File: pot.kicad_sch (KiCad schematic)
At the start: 1 part

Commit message: started to work on power part
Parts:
- gave numbers to parts that had none: 1
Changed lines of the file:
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@@
   (symbol (lib_id "power:GND") (at 112.395 92.075 0) (unit 1)
     (in_bom yes) (on_board yes) (fields_autoplaced)
-    (property "Reference" "#PWR?" (id 0) (at 112.395 98.425 0)
+    (property "Reference" "#PWR034" (id 0) (at 112.395 98.425 0)
       (effects (font (size 1.27 1.27)) hide)
     )
@@
   (symbol (lib_id "eurorack:Pot_500") (at 112.395 86.995 0) (unit 1)
     (in_bom yes) (on_board yes) (fields_autoplaced)
-    (property "Reference" "RV?" (id 0) (at 110.49 85.7249 0)
+    (property "Reference" "RV3" (id 0) (at 110.49 85.7249 0)
       (effects (font (size 1.27 1.27)) (justify right))
     )
@@
   (symbol (lib_id "eurorack:+2V048") (at 112.395 81.915 0) (unit 1)
     (in_bom yes) (on_board yes) (fields_autoplaced)
-    (property "Reference" "#PWR?" (id 0) (at 112.395 79.375 0)
+    (property "Reference" "#PWR033" (id 0) (at 112.395 79.375 0)
       (effects (font (size 1.27 1.27)) hide)
     )

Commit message: working on powers
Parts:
- renumbered RV3 to RV10
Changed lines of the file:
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@@
     (effects (font (size 1.27 1.27)) (justify left))
   )
-  (symbol (lib_id "power:GND") (at 112.395 92.075 0) (unit 1)
+  (symbol (lib_id "power:GND") (at 112.395 92.075 0)
     (in_bom yes) (on_board yes) (fields_autoplaced)
-    (property "Reference" "#PWR034" (id 0) (at 112.395 98.425 0)
+    (property "Reference" "#PWR048" (id 0) (at 112.395 98.425 0)
       (effects (font (size 1.27 1.27)) hide)
     )
@@
     (pin "1")
   )
-  (symbol (lib_id "eurorack:Pot_500") (at 112.395 86.995 0) (unit 1)
+  (symbol (lib_id "eurorack:Pot_500") (at 112.395 86.995 0)
     (in_bom yes) (on_board yes) (fields_autoplaced)
-    (property "Reference" "RV3" (id 0) (at 110.49 85.7249 0)
+    (property "Reference" "RV10" (id 0) (at 110.49 85.7249 0)
       (effects (font (size 1.27 1.27)) (justify right))
     )
@@
     (pin "3")
   )
-  (symbol (lib_id "eurorack:+2V048") (at 112.395 81.915 0) (unit 1)
+  (symbol (lib_id "eurorack:+2V048") (at 112.395 81.915 0)
     (in_bom yes) (on_board yes) (fields_autoplaced)
-    (property "Reference" "#PWR033" (id 0) (at 112.395 79.375 0)
+    (property "Reference" "#PWR047" (id 0) (at 112.395 79.375 0)
       (effects (font (size 1.27 1.27)) hide)
     )

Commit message: WIP
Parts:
- renumbered RV10 to RV3
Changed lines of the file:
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@@
     (effects (font (size 1.27 1.27)) (justify left))
   )
-  (symbol (lib_id "power:GND") (at 112.395 92.075 0)
+  (symbol (lib_id "power:GND") (at 112.395 92.075 0) (unit 1)
     (in_bom yes) (on_board yes) (fields_autoplaced)
-    (property "Reference" "#PWR048" (id 0) (at 112.395 98.425 0)
+    (property "Reference" "#PWR034" (id 0) (at 112.395 98.425 0)
       (effects (font (size 1.27 1.27)) hide)
     )
@@
     (pin "1")
   )
-  (symbol (lib_id "eurorack:Pot_500") (at 112.395 86.995 0)
+  (symbol (lib_id "eurorack:Pot_500") (at 112.395 86.995 0) (unit 1)
     (in_bom yes) (on_board yes) (fields_autoplaced)
-    (property "Reference" "RV10" (id 0) (at 110.49 85.7249 0)
+    (property "Reference" "RV3" (id 0) (at 110.49 85.7249 0)
       (effects (font (size 1.27 1.27)) (justify right))
     )
@@
     (pin "3")
   )
-  (symbol (lib_id "eurorack:+2V048") (at 112.395 81.915 0)
+  (symbol (lib_id "eurorack:+2V048") (at 112.395 81.915 0) (unit 1)
     (in_bom yes) (on_board yes) (fields_autoplaced)
-    (property "Reference" "#PWR047" (id 0) (at 112.395 79.375 0)
+    (property "Reference" "#PWR033" (id 0) (at 112.395 79.375 0)
       (effects (font (size 1.27 1.27)) hide)
     )

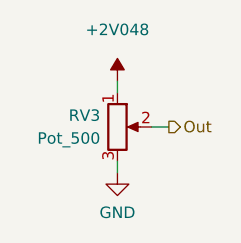
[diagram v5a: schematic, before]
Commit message: cleaning into modules
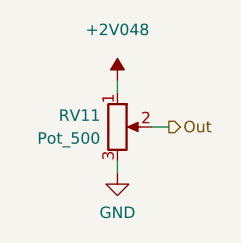
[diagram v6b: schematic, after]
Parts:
- renumbered RV3 to RV11
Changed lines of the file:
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@@
     (effects (font (size 1.27 1.27)) (justify left))
   )
-  (symbol (lib_id "power:GND") (at 112.395 92.075 0) (unit 1)
+  (symbol (lib_id "power:GND") (at 112.395 92.075 0)
     (in_bom yes) (on_board yes) (fields_autoplaced)
-    (property "Reference" "#PWR040" (id 0) (at 112.395 98.425 0)
+    (property "Reference" "#PWR083" (id 0) (at 112.395 98.425 0)
       (effects (font (size 1.27 1.27)) hide)
     )
@@
     (pin "1")
   )
-  (symbol (lib_id "eurorack:Pot_500") (at 112.395 86.995 0) (unit 1)
+  (symbol (lib_id "eurorack:Pot_500") (at 112.395 86.995 0)
     (in_bom yes) (on_board yes) (fields_autoplaced)
-    (property "Reference" "RV3" (id 0) (at 110.49 85.7249 0)
+    (property "Reference" "RV11" (id 0) (at 110.49 85.7249 0)
       (effects (font (size 1.27 1.27)) (justify right))
     )
@@
     (pin "3")
   )
-  (symbol (lib_id "eurorack:+2V048") (at 112.395 81.915 0) (unit 1)
+  (symbol (lib_id "eurorack:+2V048") (at 112.395 81.915 0)
     (in_bom yes) (on_board yes) (fields_autoplaced)
-    (property "Reference" "#PWR039" (id 0) (at 112.395 79.375 0)
+    (property "Reference" "#PWR082" (id 0) (at 112.395 79.375 0)
       (effects (font (size 1.27 1.27)) hide)
     )

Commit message: working on AD inputs
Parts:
- added D26: BAS 85 VIS, Diode_SMD:D_MiniMELF, symbol eurorack:BAS 85 VIS
- added R60: R-10k-1206, Resistor_SMD:R_1206_3216Metric_Pad1.30x1.75mm_HandSolder, symbol eurorack:R-10k-1206
- added R61: R-2k-1206, Resistor_SMD:R_1206_3216Metric_Pad1.30x1.75mm_HandSolder, symbol eurorack:R-2k-1206
- added U25: LUM-1502-03_3.5mm_mono_vertical_jack, eurorack:LUM 1502-03, symbol eurorack:LUM-1502-03_3.5mm_mono_vertical_jack
- added U26 (x3): LM358, Package_SO:SO-8_3.9x4.9mm_P1.27mm, symbol eurorack:LM358
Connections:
- net GND: now also R61.2, U25.S, U26.3 (+)
- net 1V25: no longer names the net of RV11.1
- net 1V25: now also U26.1, U26.2 (-)
- new net: D26.1 (A), U25.T
- new net: D26.2 (K), R60.1
- new net: R60.2, R61.1, U26.3 (+)
- new net: U26.1, U26.2 (-)
- new net +12V: U25.TN
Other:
- moved on the sheet: RV11
